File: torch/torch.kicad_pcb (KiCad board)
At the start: 2 copper layers, 66.4 x 24.3 mm, 5 parts, among them SW1 SW_DPST_x2

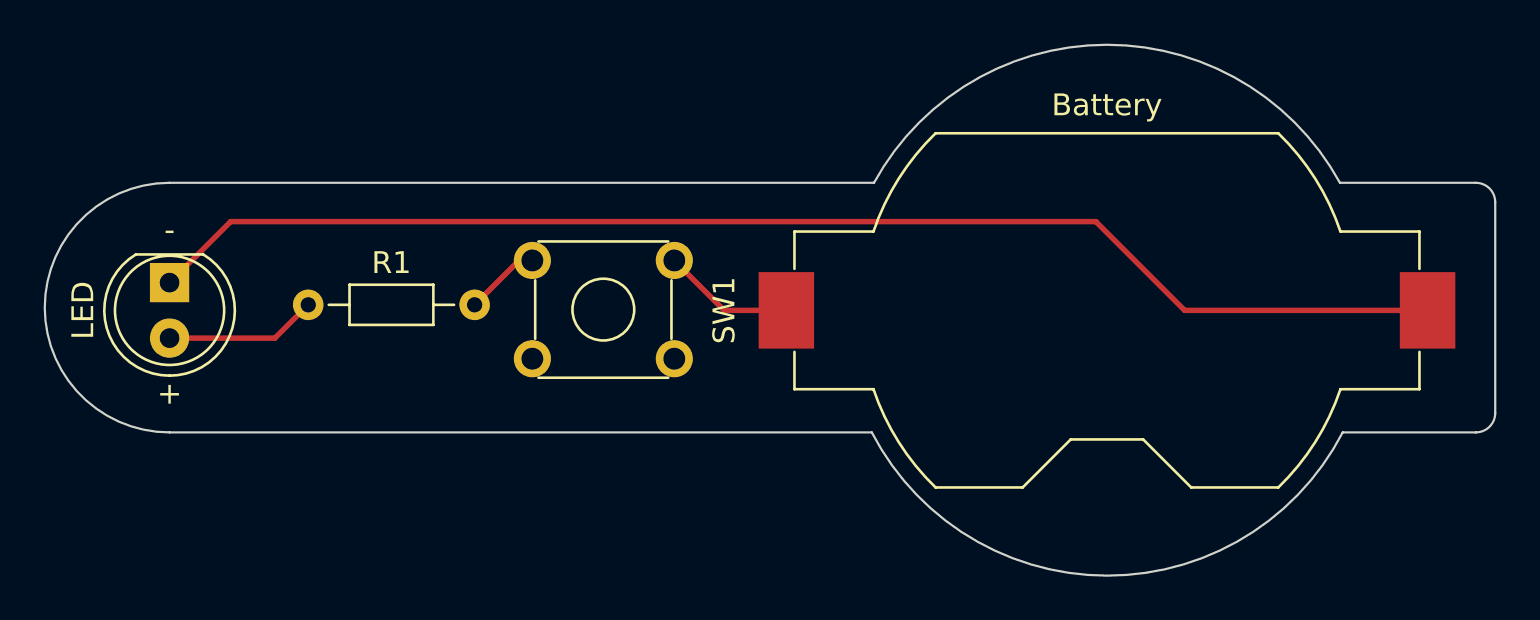
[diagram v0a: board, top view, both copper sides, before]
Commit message: feat: center resistor
Signed-off-by: Matt Gleich <git@mattglei.ch>
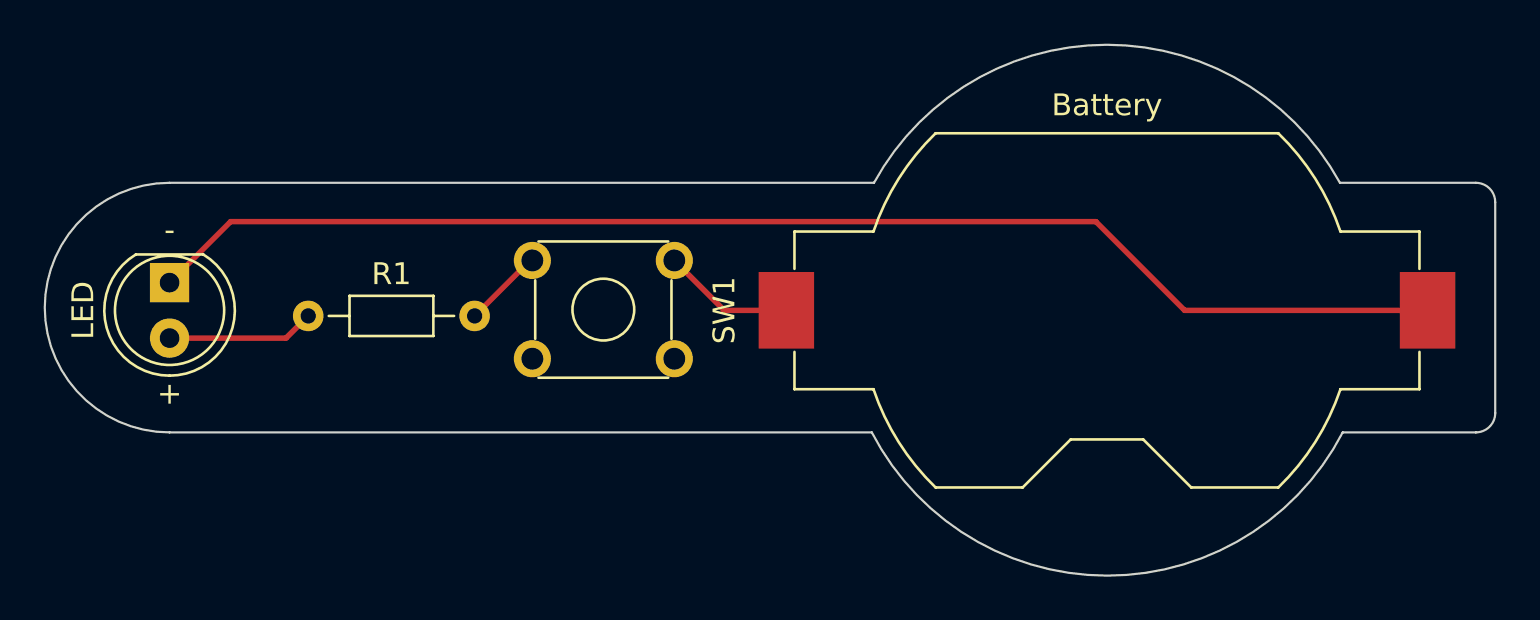
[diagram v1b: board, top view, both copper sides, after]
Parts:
- moved R1 0.51 mm to (131.1, 76.5)
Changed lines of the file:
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@@
   (net 4 "Net-(R1-Pad2)")
   (footprint "Resistor_THT:R_Axial_DIN0204_L3.6mm_D1.6mm_P7.62mm_Horizontal" (layer "F.Cu")
-    (at 131.064 75.946)
+    (at 131.064 76.454)
     (descr "Resistor, Axial_DIN0204 series, Axial, Horizontal, pin pitch=7.62mm, 0.167W, length*diameter=3.6*1.6mm^2, http://cdn-reichelt.de/documents/datenblatt/B400/1_4W%23YAG.pdf")
     (tags "Resistor Axial_DIN0204 series Axial Horizontal pin pitch 7.62mm 0.167W length 3.6mm diameter 1.6mm")
@@
   (gr_arc (start 185.42 80.899) (mid 185.159618 81.527618) (end 184.531 81.788) (layer "Edge.Cuts") (width 0.1))
   (gr_line (start 185.42 80.899) (end 185.42 71.247) (layer "Edge.Cuts") (width 0.1))
-  (gr_arc (start 178.435 81.788) (mid 167.653609 88.347285) (end 156.872217 81.788) (layer "Edge.Cuts") (width 0.1))
+  (gr_arc (start 178.435 81.788) (mid 167.653609 88.347284) (end 156.872217 81.788) (layer "Edge.Cuts") (width 0.1))
   (gr_arc (start 124.714 81.788) (mid 118.999 76.073) (end 124.714 70.358) (layer "Edge.Cuts") (width 0.1))
   (gr_line (start 156.972 70.358) (end 124.714 70.358) (layer "Edge.Cuts") (width 0.1))
@@
   (segment (start 127.508 72.136) (end 167.132 72.136) (width 0.25) (layer "F.Cu") (net 2))
   (segment (start 124.714 74.93) (end 127.508 72.136) (width 0.25) (layer "F.Cu") (net 2))
-  (segment (start 124.714 77.47) (end 129.54 77.47) (width 0.25) (layer "F.Cu") (net 3))
-  (segment (start 129.54 77.47) (end 131.064 75.946) (width 0.25) (layer "F.Cu") (net 3))
-  (segment (start 140.716 73.914) (end 141.328 73.914) (width 0.25) (layer "F.Cu") (net 4))
-  (segment (start 138.684 75.946) (end 140.716 73.914) (width 0.25) (layer "F.Cu") (net 4))
+  (segment (start 124.714 77.47) (end 130.048 77.47) (width 0.25) (layer "F.Cu") (net 3))
+  (segment (start 130.048 77.47) (end 131.064 76.454) (width 0.25) (layer "F.Cu") (net 3))
+  (segment (start 141.224 73.914) (end 141.328 73.914) (width 0.25) (layer "F.Cu") (net 4))
+  (segment (start 138.684 76.454) (end 141.224 73.914) (width 0.25) (layer "F.Cu") (net 4))
 )

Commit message: feat: dimensions
Signed-off-by: Matt Gleich <git@mattglei.ch>
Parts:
- moved R1 0.63 mm to (130.4, 76.5)
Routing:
- net Net-(R1-Pad2): track 3.70 -> 4.33 mm
- net /LED_anode: track 6.77 -> 6.14 mm
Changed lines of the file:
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@@
   (setup
     (pad_to_mask_clearance 0)
+    (aux_axis_origin 167.64 64.037139)
     (pcbplotparams
       (layerselection 0x00010fc_ffffffff)
@@
   (net 4 "Net-(R1-Pad2)")
   (footprint "Resistor_THT:R_Axial_DIN0204_L3.6mm_D1.6mm_P7.62mm_Horizontal" (layer "F.Cu")
-    (at 131.064 76.454)
+    (at 130.429 76.454)
     (descr "Resistor, Axial_DIN0204 series, Axial, Horizontal, pin pitch=7.62mm, 0.167W, length*diameter=3.6*1.6mm^2, http://cdn-reichelt.de/documents/datenblatt/B400/1_4W%23YAG.pdf")
     (tags "Resistor Axial_DIN0204 series Axial Horizontal pin pitch 7.62mm 0.167W length 3.6mm diameter 1.6mm")
@@
     (effects (font (size 1 1) (thickness 0.15)))
   )
+  (dimension (type aligned) (layer "Dwgs.User")
+    (pts (xy 118.999 76.073) (xy 185.42 76.073))
+    (height -18.542)
+    (gr_text "66.4210 mm" (at 152.2095 55.731) (layer "Dwgs.User")
+      (effects (font (size 1.5 1.5) (thickness 0.3)))
+    )
+    (format (units 3) (units_format 1) (precision 4))
+    (style (thickness 0.2) (arrow_length 1.27) (text_position_mode 0) (extension_height 0.58642) (extension_offset 0.5) keep_text_aligned)
+  )
+  (dimension (type aligned) (layer "Dwgs.User")
+    (pts (xy 167.64 64.037139) (xy 167.653609 88.347284))
+    (height -35.17183)
+    (gr_text "24.3101 mm" (at 204.618628 76.171514 270.0320722) (layer "Dwgs.User")
+      (effects (font (size 1.5 1.5) (thickness 0.3)))
+    )
+    (format (units 3) (units_format 1) (precision 4))
+    (style (thickness 0.2) (arrow_length 1.27) (text_position_mode 0) (extension_height 0.58642) (extension_offset 0.5) keep_text_aligned)
+  )
   (segment (start 150.114 76.2) (end 152.96 76.2) (width 0.25) (layer "F.Cu") (net 1))
   (segment (start 147.828 73.914) (end 150.114 76.2) (width 0.25) (layer "F.Cu") (net 1))
@@
   (segment (start 127.508 72.136) (end 167.132 72.136) (width 0.25) (layer "F.Cu") (net 2))
   (segment (start 124.714 74.93) (end 127.508 72.136) (width 0.25) (layer "F.Cu") (net 2))
-  (segment (start 124.714 77.47) (end 130.048 77.47) (width 0.25) (layer "F.Cu") (net 3))
-  (segment (start 130.048 77.47) (end 131.064 76.454) (width 0.25) (layer "F.Cu") (net 3))
-  (segment (start 141.224 73.914) (end 141.328 73.914) (width 0.25) (layer "F.Cu") (net 4))
-  (segment (start 138.684 76.454) (end 141.224 73.914) (width 0.25) (layer "F.Cu") (net 4))
+  (segment (start 124.714 77.47) (end 129.413 77.47) (width 0.25) (layer "F.Cu") (net 3))
+  (segment (start 129.413 77.47) (end 130.429 76.454) (width 0.25) (layer "F.Cu") (net 3))
+  (segment (start 140.589 73.914) (end 141.328 73.914) (width 0.25) (layer "F.Cu") (net 4))
+  (segment (start 138.049 76.454) (end 140.589 73.914) (width 0.25) (layer "F.Cu") (net 4))
 )

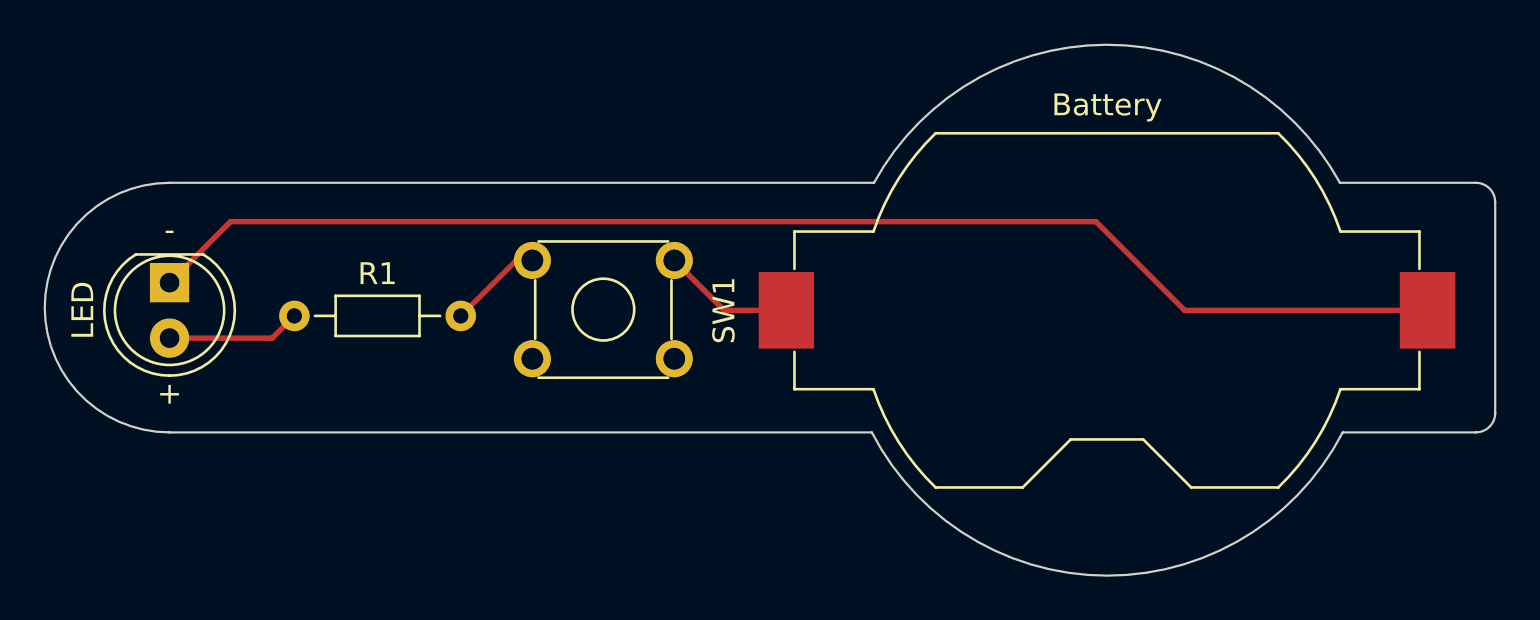
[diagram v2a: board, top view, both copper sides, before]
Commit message: feat: align items
Signed-off-by: Matt Gleich <git@mattglei.ch>
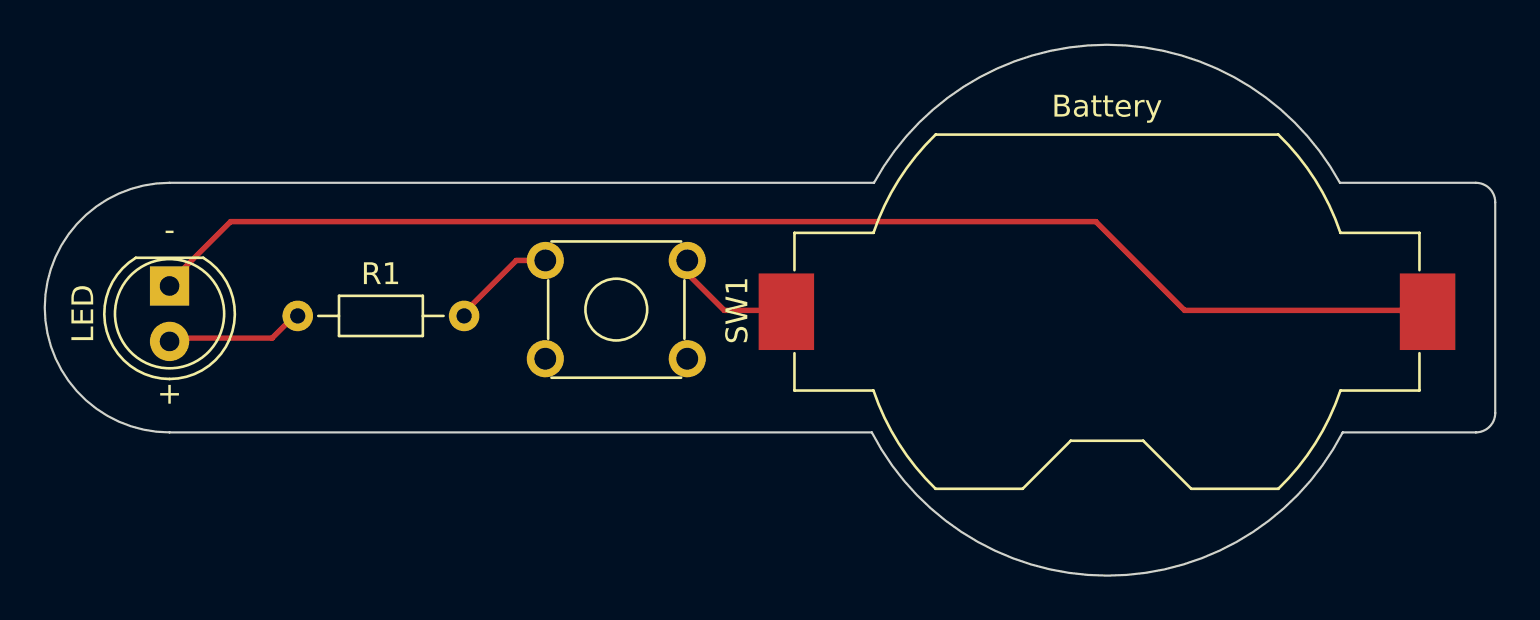
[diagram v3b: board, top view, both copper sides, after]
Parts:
- moved SW1 0.59 mm to (141.9, 73.9)
- moved R1 0.15 mm to (130.6, 76.5)
- moved D1 0.15 mm to (124.7, 75.1)
- moved BT1 0.06 mm to (167.6, 76.3)
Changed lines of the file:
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@@
   (net 4 "Net-(R1-Pad2)")
   (footprint "Resistor_THT:R_Axial_DIN0204_L3.6mm_D1.6mm_P7.62mm_Horizontal" (layer "F.Cu")
-    (at 130.429 76.454)
+    (at 130.582666 76.453998)
     (descr "Resistor, Axial_DIN0204 series, Axial, Horizontal, pin pitch=7.62mm, 0.167W, length*diameter=3.6*1.6mm^2, http://cdn-reichelt.de/documents/datenblatt/B400/1_4W%23YAG.pdf")
     (tags "Resistor Axial_DIN0204 series Axial Horizontal pin pitch 7.62mm 0.167W length 3.6mm diameter 1.6mm")
@@
   )
   (footprint "Button_Switch_THT:SW_TH_Tactile_Omron_B3F-10xx" (layer "F.Cu")
-    (at 141.328 73.914)
+    (at 141.921332 73.914)
     (descr "SW_TH_Tactile_Omron_B3F-10xx_https://www.omron.com/ecb/products/pdf/en-b3f.pdf")
     (tags "Omron B3F-10xx")
@@
   )
   (footprint "Battery:BatteryHolder_Keystone_1058_1x2032" (layer "F.Cu")
-    (at 167.64 76.2)
+    (at 167.64 76.260666)
     (descr "http://www.keyelco.com/product-pdf.cfm?p=14028")
     (tags "Keystone type 1058 coin cell retainer")
@@
   )
   (footprint "LED_THT:LED_D5.0mm" (layer "F.Cu")
-    (at 124.714 74.93 -90)
+    (at 124.714 75.082332 -90)
     (descr "LED, diameter 5.0mm, 2 pins, http://cdn-reichelt.de/documents/datenblatt/A500/LL-504BC2E-009.pdf")
     (tags "LED diameter 5.0mm 2 pins")
